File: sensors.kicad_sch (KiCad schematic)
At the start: 12 parts, among them U2 SAM-M10Q-00B, U3 LSM6DSOX, U4 LIS2MDL, U7 LPS22DFTR

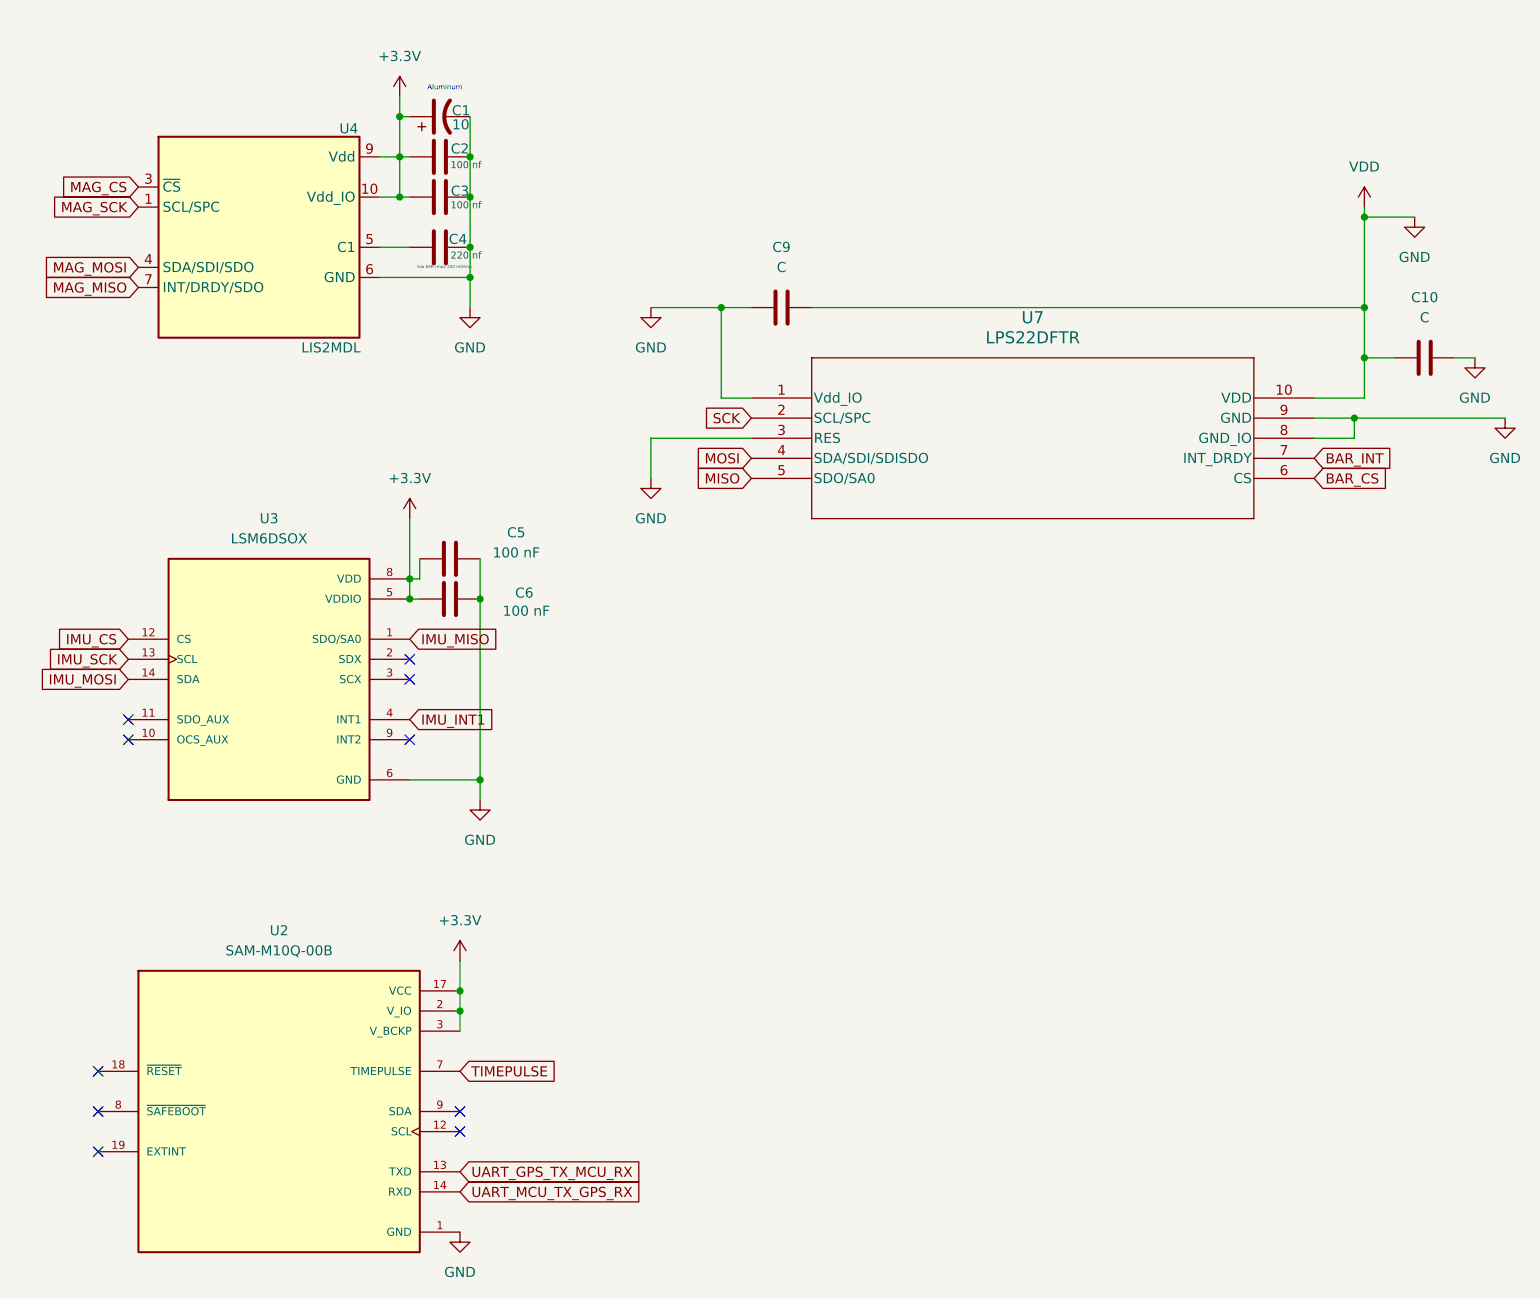
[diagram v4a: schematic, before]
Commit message: Worked on fixing the Barrometer changes
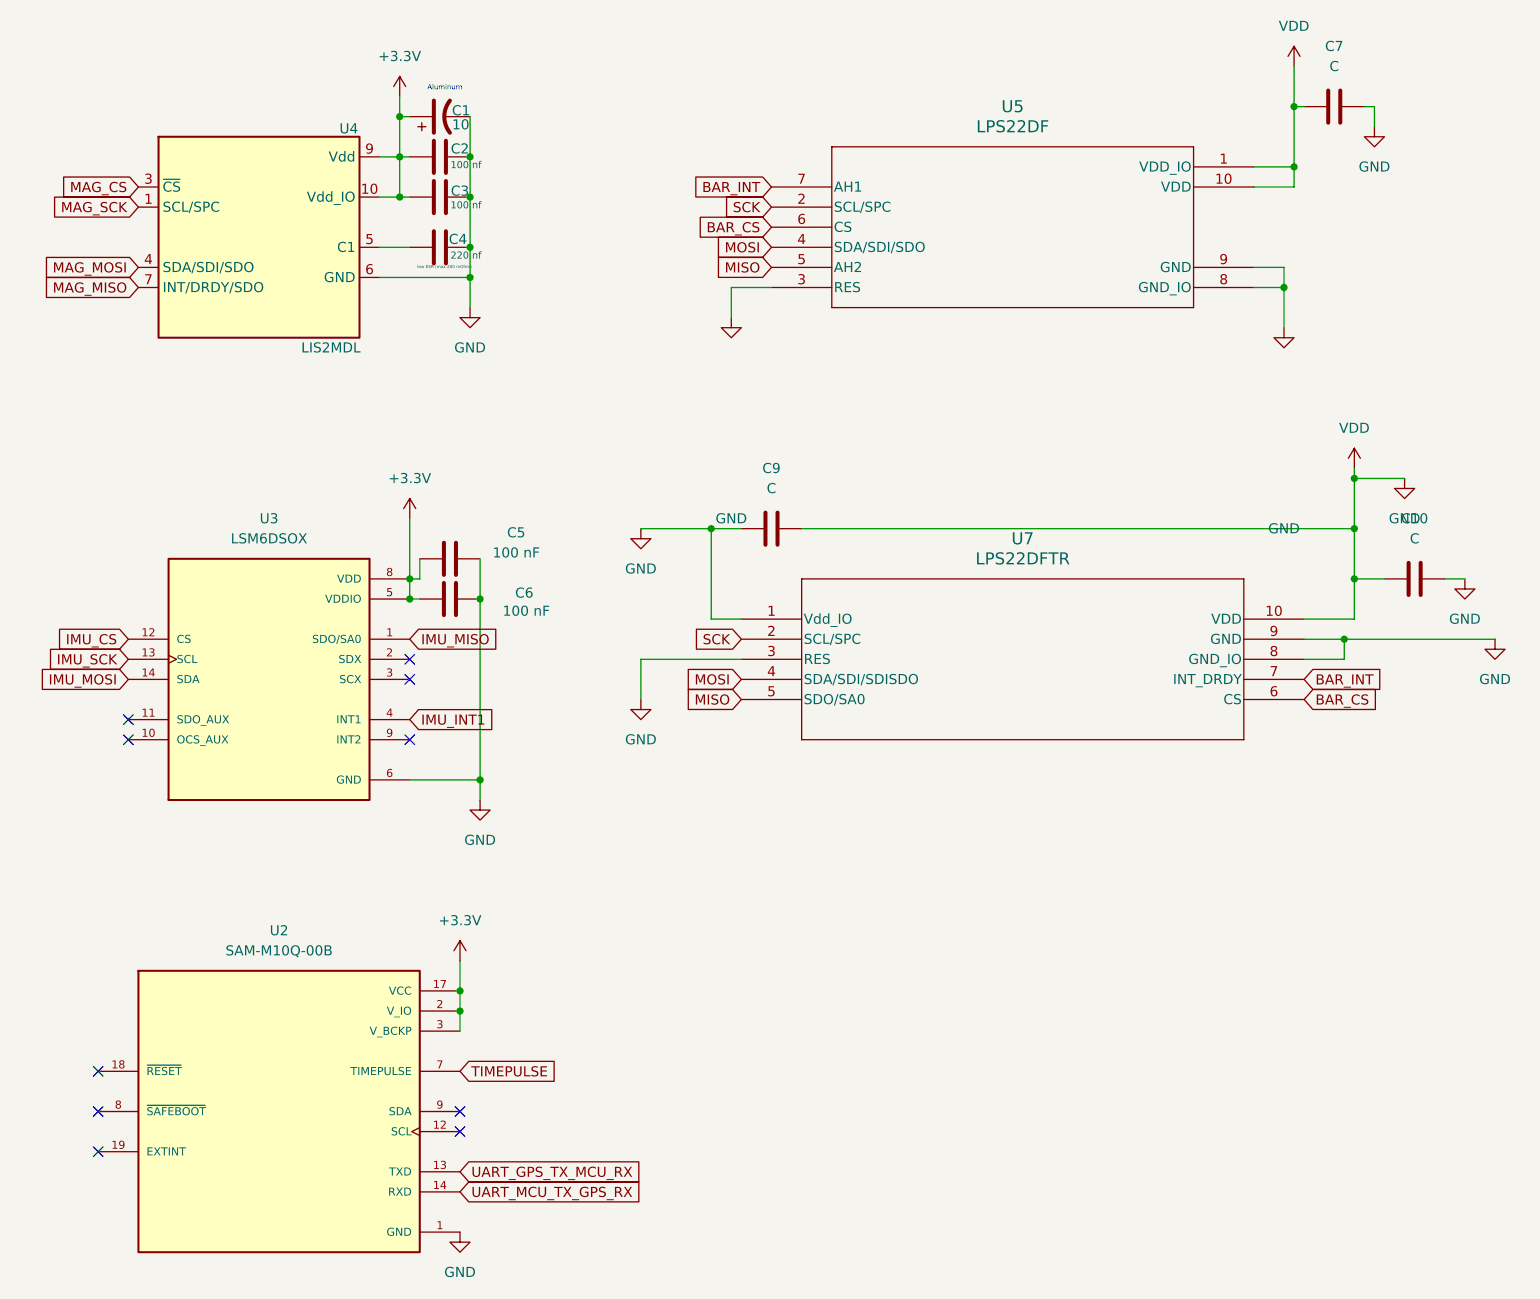
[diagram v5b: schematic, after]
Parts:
- added C7: C, Capacitor_SMD:C_0603_1608Metric, symbol Device:C
- added U5: LPS22DF, HLGA_10L_STM, symbol LPS22DFTR:LPS22DF
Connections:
- net BAR_CS: now also U5.6 (CS)
- net BAR_INT: now also U5.7 (AH1)
- net GND: now also C7.1, C7.2, U5.1 (VDD_IO), U5.10 (VDD), U5.3 (RES), U5.8 (GND_IO), U5.9 (GND)
- net MISO: now also U5.5 (AH2)
- net MOSI: now also U5.4 (SDA/SDI/SDO)
- net SCK: now also U5.2 (SCL/SPC)
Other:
- moved on the sheet: C10, C9, U7
